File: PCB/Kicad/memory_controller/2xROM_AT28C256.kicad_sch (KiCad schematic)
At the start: 4 parts, among them U25 AT28C256-15PU

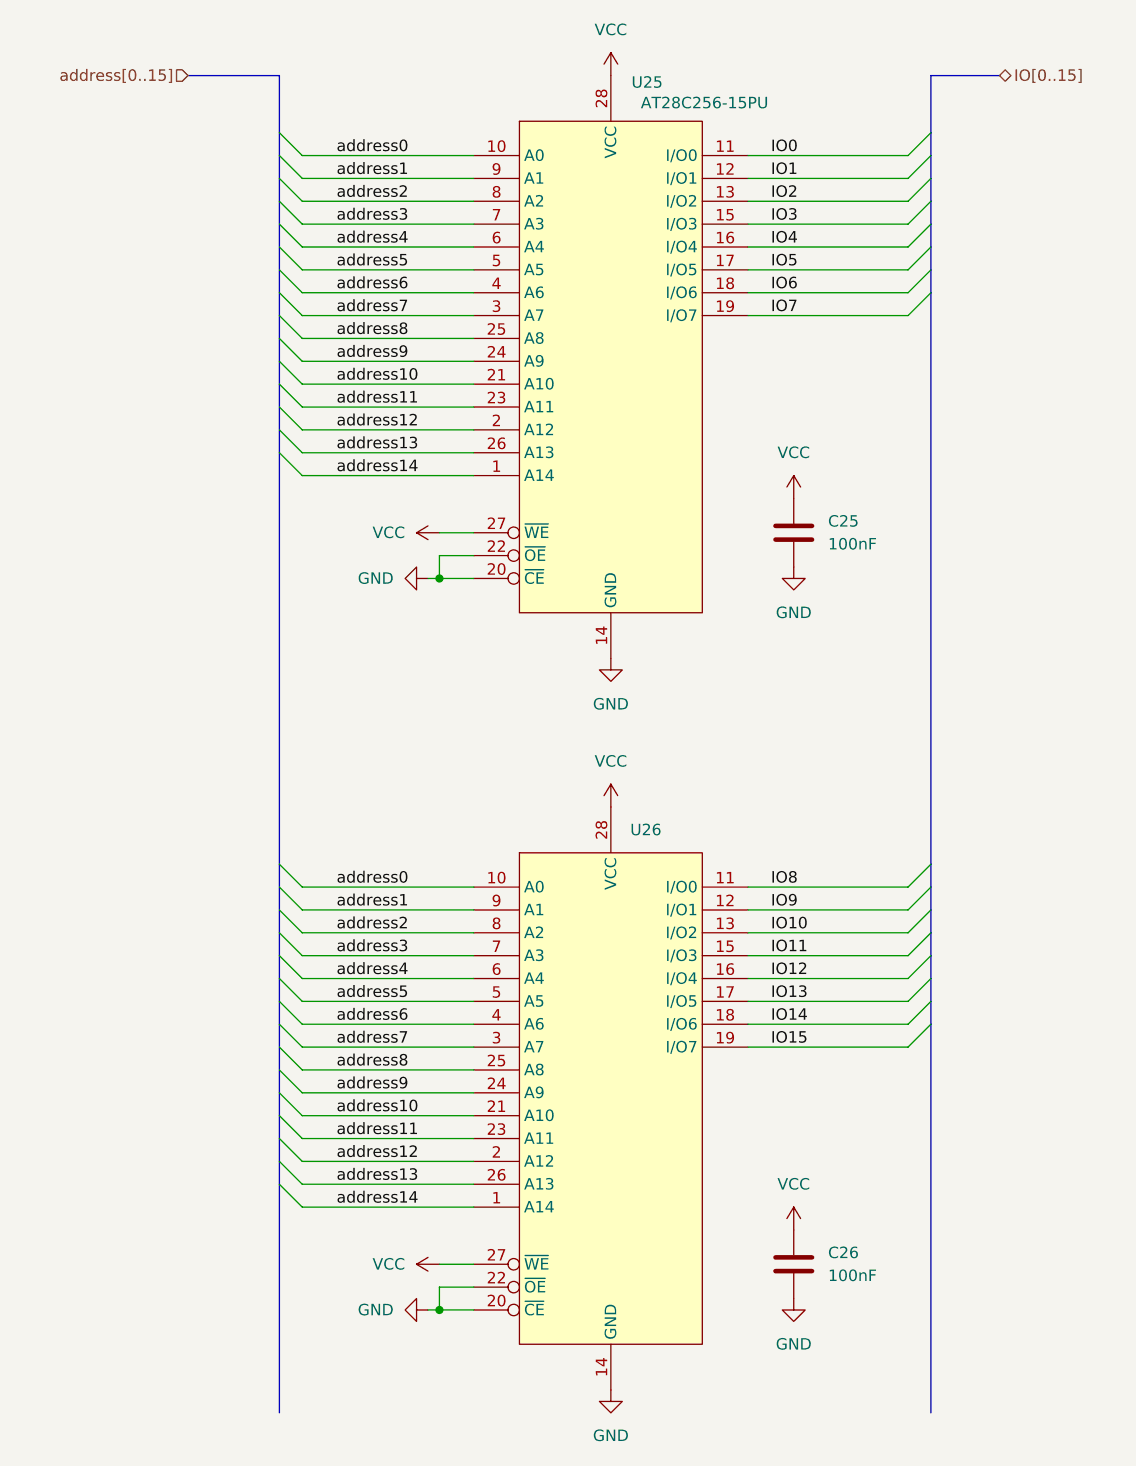
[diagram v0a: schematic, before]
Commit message: memory controler fix
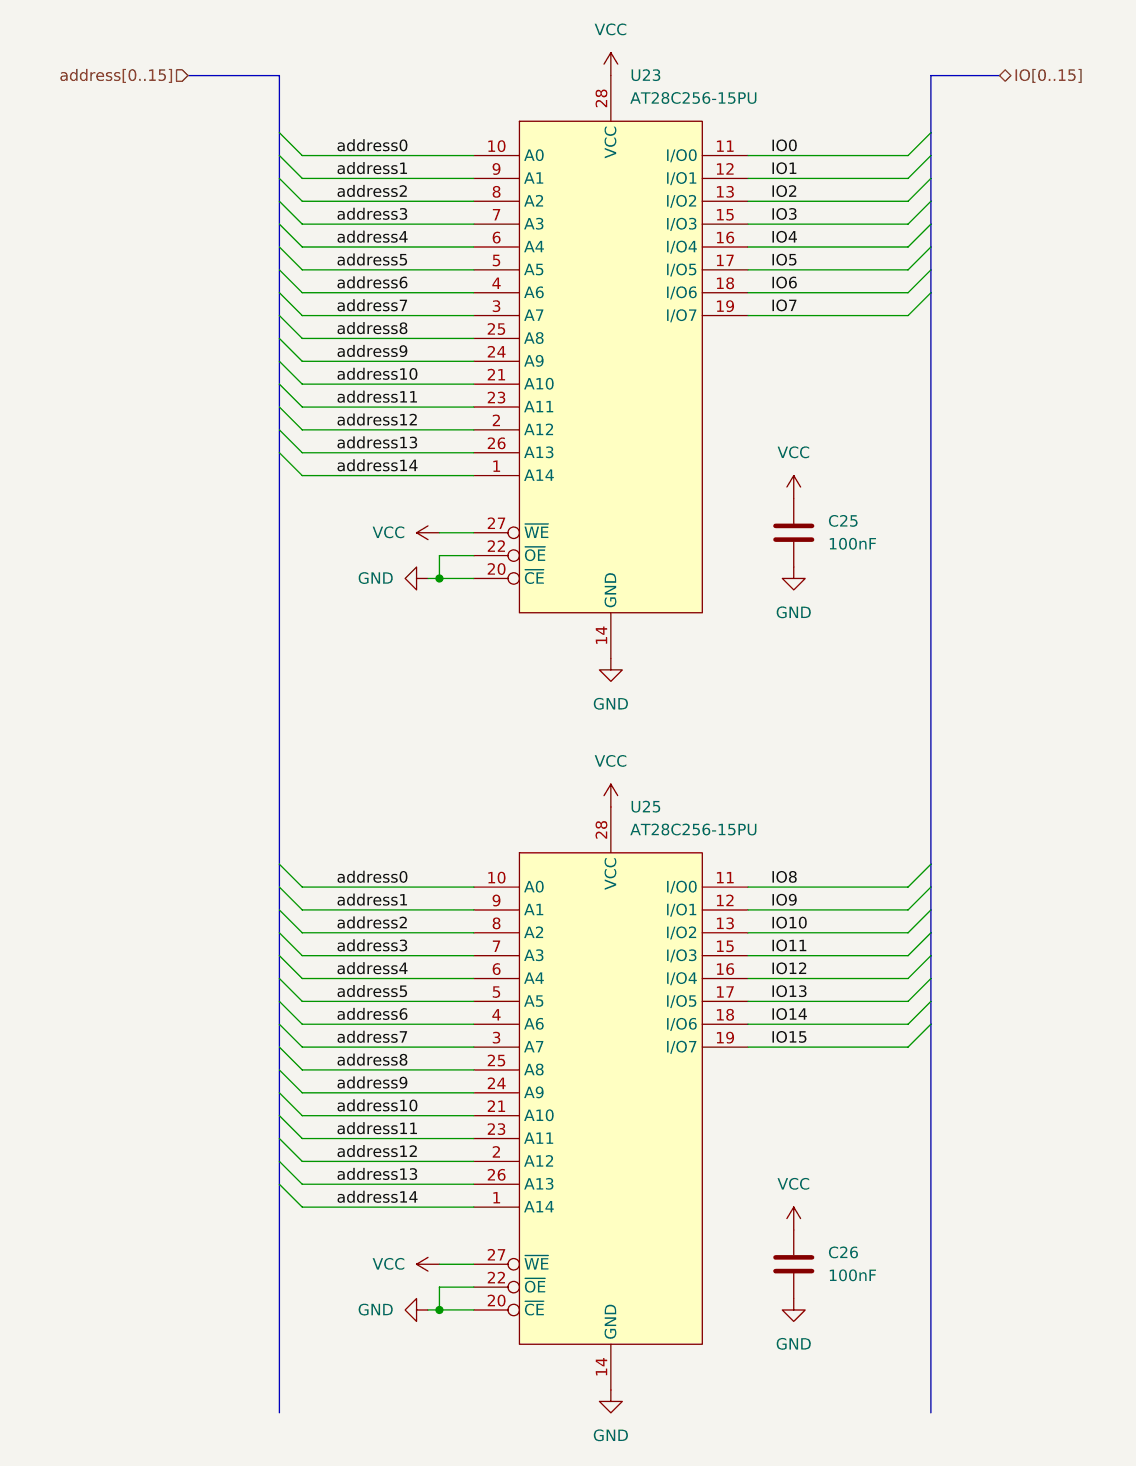
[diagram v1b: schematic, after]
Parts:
- removed U25: AT28C256-15PU, symbol mALUch_lib:ROM_AT28C256
- removed U26: ~, symbol mALUch_lib:ROM_AT28C256
- added U23, U25: AT28C256-15PU, symbol mALUch_lib:ROM__AT28C256-15PU
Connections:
- net GND: now also U23.14 (GND), U23.20 (~{CE}), U23.22 (~{OE}), U25.14 (GND), U25.20 (~{CE}), U25.22 (~{OE})
- net IO0: now also U23.11 (I/O0)
- net IO1: now also U23.12 (I/O1)
- net IO10: now also U25.13 (I/O2)
- net IO11: now also U25.15 (I/O3)
- net IO12: now also U25.16 (I/O4)
- net IO13: now also U25.17 (I/O5)
- net IO14: now also U25.18 (I/O6)
- net IO15: now also U25.19 (I/O7)
- net IO2: now also U23.13 (I/O2)
- net IO3: now also U23.15 (I/O3)
- net IO4: now also U23.16 (I/O4)
- net IO5: now also U23.17 (I/O5)
- net IO6: now also U23.18 (I/O6)
- net IO7: now also U23.19 (I/O7)
- net IO8: now also U25.11 (I/O0)
- net IO9: now also U25.12 (I/O1)
- net VCC: now also U23.27 (~{WE}), U23.28 (VCC), U25.27 (~{WE}), U25.28 (VCC)
- net address0: now also U23.10 (A0), U25.10 (A0)
- net address1: now also U23.9 (A1), U25.9 (A1)
- net address10: now also U23.21 (A10), U25.21 (A10)
- net address11: now also U23.23 (A11), U25.23 (A11)
- net address12: now also U23.2 (A12), U25.2 (A12)
- net address13: now also U23.26 (A13), U25.26 (A13)
- net address14: now also U23.1 (A14), U25.1 (A14)
- net address2: now also U23.8 (A2), U25.8 (A2)
- net address3: now also U23.7 (A3), U25.7 (A3)
- net address4: now also U23.6 (A4), U25.6 (A4)
- net address5: now also U23.5 (A5), U25.5 (A5)
- net address6: now also U23.4 (A6), U25.4 (A6)
- net address7: now also U23.3 (A7), U25.3 (A7)
- net address8: now also U23.25 (A8), U25.25 (A8)
- net address9: now also U23.24 (A9), U25.24 (A9)

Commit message: kicad fix
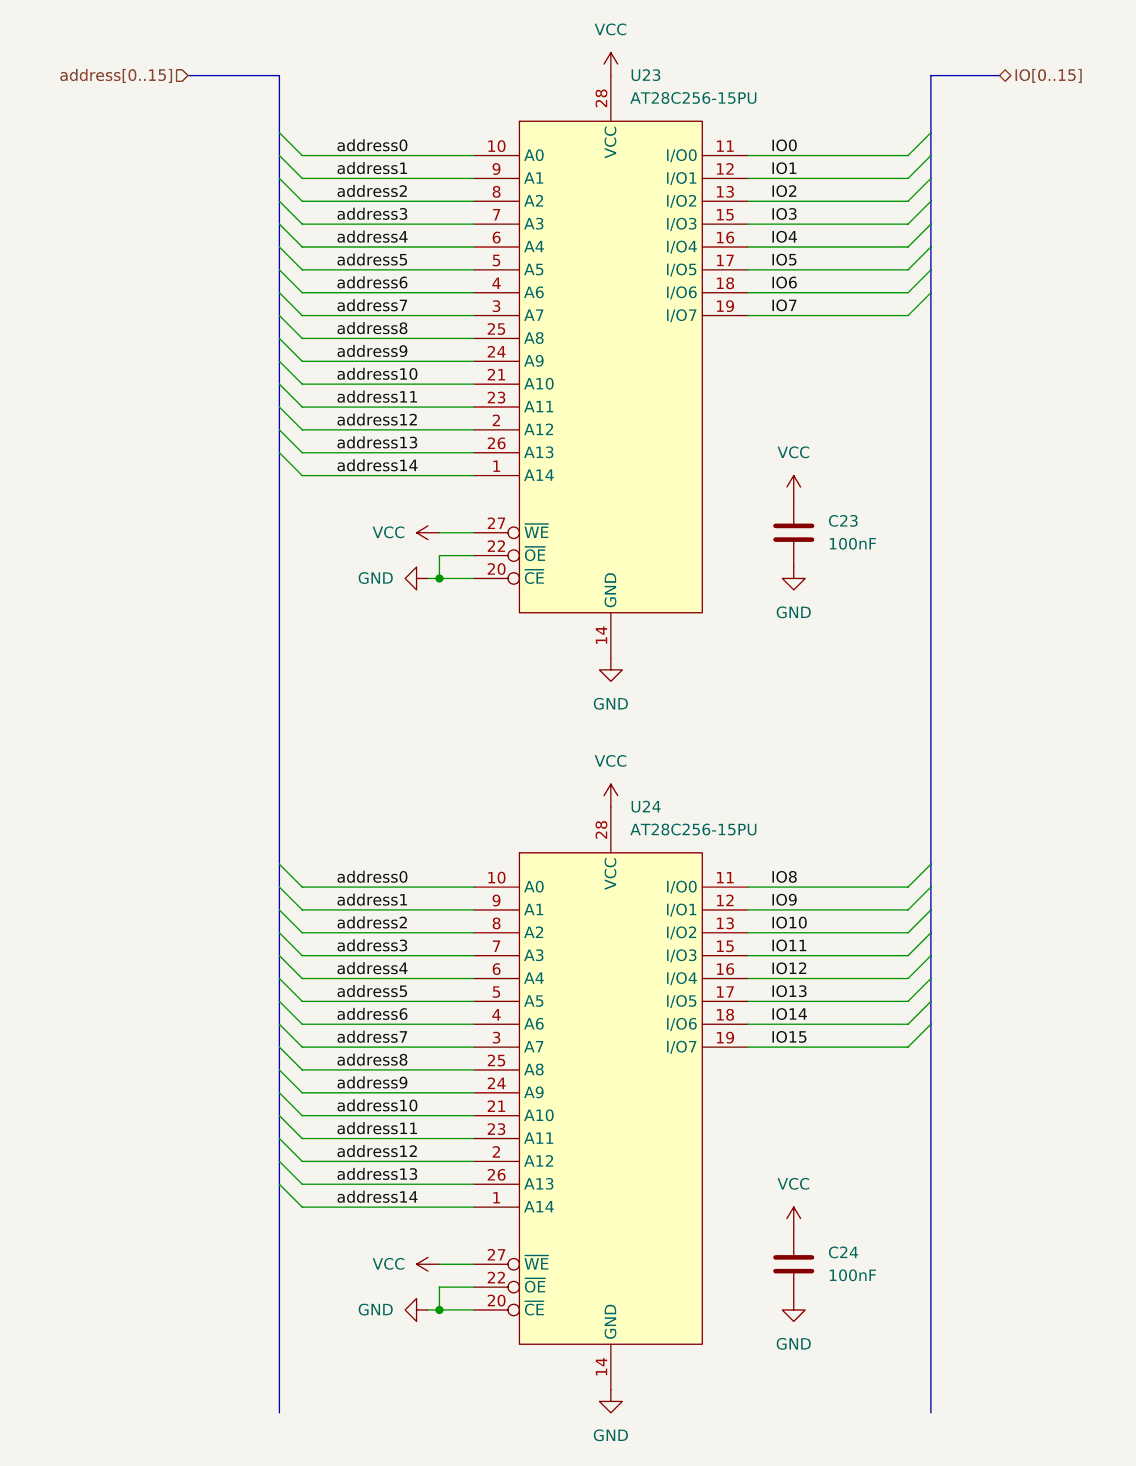
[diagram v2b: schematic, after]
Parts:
- renumbered C25 to C23, C26 to C24, U25 to U24
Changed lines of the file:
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@@
 		(dnp no)
 		(fields_autoplaced yes)
-		(property "Reference" "#PWR0130"
+		(property "Reference" "#PWR0120"
 			(at 104.14 181.61 0)
 			(effects
@@
 			(project "memory_controller"
 				(path "/dccec861-b967-466c-843e-d6d1ad6064ce/3e52e97d-2d91-445f-b76b-e1b0d1dc86b1"
-					(reference "#PWR0130")
+					(reference "#PWR0120")
 					(unit 1)
 				)
@@
 		(dnp no)
 		(fields_autoplaced yes)
-		(property "Reference" "#PWR0134"
+		(property "Reference" "#PWR0124"
 			(at 124.46 171.45 0)
 			(effects
@@
 			(project "memory_controller"
 				(path "/dccec861-b967-466c-843e-d6d1ad6064ce/3e52e97d-2d91-445f-b76b-e1b0d1dc86b1"
-					(reference "#PWR0134")
+					(reference "#PWR0124")
 					(unit 1)
 				)
@@
 		(dnp no)
 		(fields_autoplaced yes)
-		(property "Reference" "#PWR0132"
+		(property "Reference" "#PWR0122"
 			(at 124.46 90.17 0)
 			(effects
@@
 			(project "memory_controller"
 				(path "/dccec861-b967-466c-843e-d6d1ad6064ce/3e52e97d-2d91-445f-b76b-e1b0d1dc86b1"
-					(reference "#PWR0132")
+					(reference "#PWR0122")
 					(unit 1)
 				)
@@
 		(dnp no)
 		(fields_autoplaced yes)
-		(property "Reference" "#PWR0128"
+		(property "Reference" "#PWR0118"
 			(at 104.14 100.33 0)
 			(effects
@@
 			(project ""
 				(path "/dccec861-b967-466c-843e-d6d1ad6064ce/3e52e97d-2d91-445f-b76b-e1b0d1dc86b1"
-					(reference "#PWR0128")
+					(reference "#PWR0118")
 					(unit 1)
 				)
@@
 		(dnp no)
 		(fields_autoplaced yes)
-		(property "Reference" "C25"
+		(property "Reference" "C23"
 			(at 128.27 78.7399 0)
 			(effects
@@
 			(project "memory_controller"
 				(path "/dccec861-b967-466c-843e-d6d1ad6064ce/3e52e97d-2d91-445f-b76b-e1b0d1dc86b1"
-					(reference "C25")
+					(reference "C23")
 					(unit 1)
 				)
@@
 		(dnp no)
 		(fields_autoplaced yes)
-		(property "Reference" "#PWR0127"
+		(property "Reference" "#PWR0117"
 			(at 104.14 33.02 0)
 			(effects
@@
 			(project ""
 				(path "/dccec861-b967-466c-843e-d6d1ad6064ce/3e52e97d-2d91-445f-b76b-e1b0d1dc86b1"
-					(reference "#PWR0127")
+					(reference "#PWR0117")
 					(unit 1)
 				)
@@
 		(dnp no)
 		(fields_autoplaced yes)
-		(property "Reference" "C26"
+		(property "Reference" "C24"
 			(at 128.27 160.0199 0)
 			(effects
@@
 			(project "memory_controller"
 				(path "/dccec861-b967-466c-843e-d6d1ad6064ce/3e52e97d-2d91-445f-b76b-e1b0d1dc86b1"
-					(reference "C26")
+					(reference "C24")
 					(unit 1)
 				)
@@
 		(dnp no)
 		(fields_autoplaced yes)
-		(property "Reference" "#PWR0124"
+		(property "Reference" "#PWR0114"
 			(at 77.47 166.37 0)
 			(effects
@@
 			(project "memory_controller"
 				(path "/dccec861-b967-466c-843e-d6d1ad6064ce/3e52e97d-2d91-445f-b76b-e1b0d1dc86b1"
-					(reference "#PWR0124")
+					(reference "#PWR0114")
 					(unit 1)
 				)
@@
 		(dnp no)
 		(fields_autoplaced yes)
-		(property "Reference" "#PWR0133"
+		(property "Reference" "#PWR0123"
 			(at 124.46 161.29 0)
 			(effects
@@
 			(project "memory_controller"
 				(path "/dccec861-b967-466c-843e-d6d1ad6064ce/3e52e97d-2d91-445f-b76b-e1b0d1dc86b1"
-					(reference "#PWR0133")
+					(reference "#PWR0123")
 					(unit 1)
 				)
@@
 		(dnp no)
 		(fields_autoplaced yes)
-		(property "Reference" "#PWR0125"
+		(property "Reference" "#PWR0115"
 			(at 88.9 80.01 0)
 			(effects
@@
 			(project "memory_controller"
 				(path "/dccec861-b967-466c-843e-d6d1ad6064ce/3e52e97d-2d91-445f-b76b-e1b0d1dc86b1"
-					(reference "#PWR0125")
+					(reference "#PWR0115")
 					(unit 1)
 				)
@@
 		(dnp no)
 		(fields_autoplaced yes)
-		(property "Reference" "#PWR0126"
+		(property "Reference" "#PWR0116"
 			(at 88.9 161.29 0)
 			(effects
@@
 			(project "memory_controller"
 				(path "/dccec861-b967-466c-843e-d6d1ad6064ce/3e52e97d-2d91-445f-b76b-e1b0d1dc86b1"
-					(reference "#PWR0126")
+					(reference "#PWR0116")
 					(unit 1)
 				)
@@
 		(dnp no)
 		(fields_autoplaced yes)
-		(property "Reference" "#PWR0123"
+		(property "Reference" "#PWR0113"
 			(at 77.47 85.09 0)
 			(effects
@@
 			(project "memory_controller"
 				(path "/dccec861-b967-466c-843e-d6d1ad6064ce/3e52e97d-2d91-445f-b76b-e1b0d1dc86b1"
-					(reference "#PWR0123")
+					(reference "#PWR0113")
 					(unit 1)
 				)
@@
 		(dnp no)
 		(fields_autoplaced yes)
-		(property "Reference" "U25"
+		(property "Reference" "U24"
 			(at 106.2833 110.49 0)
 			(effects
@@
 			(project ""
 				(path "/dccec861-b967-466c-843e-d6d1ad6064ce/3e52e97d-2d91-445f-b76b-e1b0d1dc86b1"
-					(reference "U25")
+					(reference "U24")
 					(unit 1)
 				)
@@
 		(dnp no)
 		(fields_autoplaced yes)
-		(property "Reference" "#PWR0129"
+		(property "Reference" "#PWR0119"
 			(at 104.14 114.3 0)
 			(effects
@@
 			(project "memory_controller"
 				(path "/dccec861-b967-466c-843e-d6d1ad6064ce/3e52e97d-2d91-445f-b76b-e1b0d1dc86b1"
-					(reference "#PWR0129")
+					(reference "#PWR0119")
 					(unit 1)
 				)
@@
 		(dnp no)
 		(fields_autoplaced yes)
-		(property "Reference" "#PWR0131"
+		(property "Reference" "#PWR0121"
 			(at 124.46 80.01 0)
 			(effects
@@
 			(project "memory_controller"
 				(path "/dccec861-b967-466c-843e-d6d1ad6064ce/3e52e97d-2d91-445f-b76b-e1b0d1dc86b1"
-					(reference "#PWR0131")
-					(unit 1)
-				)
+					(reference "#PWR0121")
+					(unit 1)
+				)

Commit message: pcb init
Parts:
- C23, C24: footprint (none) -> Capacitor_SMD:C_0402_1005Metric
- U23, U24: footprint (none) -> Package_DIP:DIP-28_W15.24mm_Socket
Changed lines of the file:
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@@
 			)
 		)
-		(property "Footprint" ""
+		(property "Footprint" "Capacitor_SMD:C_0402_1005Metric"
 			(at 123.4948 76.2 0)
 			(effects
@@
 			)
 		)
-		(property "Footprint" ""
+		(property "Footprint" "Capacitor_SMD:C_0402_1005Metric"
 			(at 123.4948 157.48 0)
 			(effects
@@
 			)
 		)
-		(property "Footprint" ""
+		(property "Footprint" "Package_DIP:DIP-28_W15.24mm_Socket"
 			(at 104.14 58.42 0)
 			(effects
@@
 			)
 		)
-		(property "Footprint" ""
+		(property "Footprint" "Package_DIP:DIP-28_W15.24mm_Socket"
 			(at 104.14 139.7 0)
 			(effects

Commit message: names
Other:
- title: 2xROM -> 2xROM AT28C256
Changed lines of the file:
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@@
 	(paper "A4")
 	(title_block
-		(title "2xROM")
+		(title "2xROM AT28C256")
+		(comment 1 "review: Hubert Wójcik")
+		(comment 2 "author: Maciej Rogoż")
 	)
 	(junction

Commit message: memory controller schematic update
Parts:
- U23, U24: now not fitted
